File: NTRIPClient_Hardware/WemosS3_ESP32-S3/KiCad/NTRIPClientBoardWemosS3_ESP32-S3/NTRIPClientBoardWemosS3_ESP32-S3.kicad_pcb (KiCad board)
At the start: 2 copper layers, 68.9 x 133 mm, 2 parts, among them U1 Wemos_S3_ESP32-S3

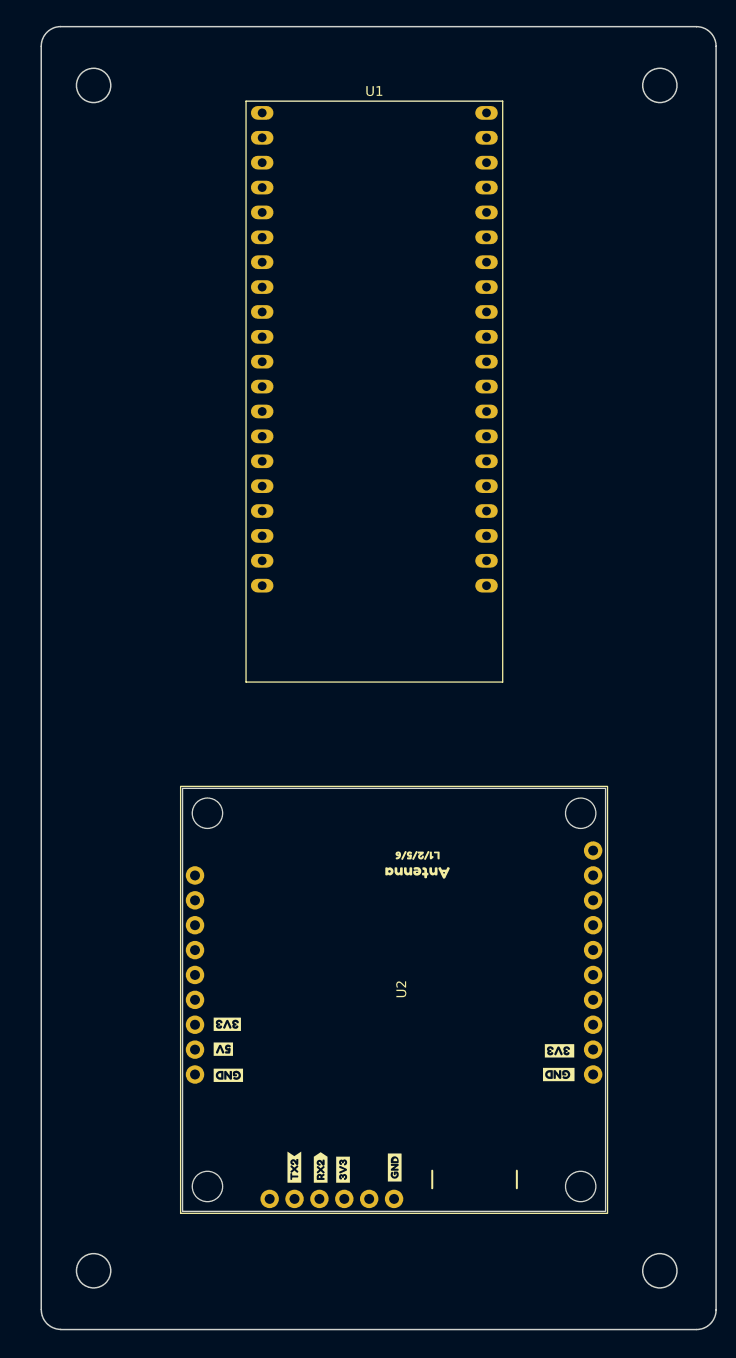
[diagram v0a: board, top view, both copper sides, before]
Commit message: Updated PCB for LOLIN S3 WEMOS board to version 1.0
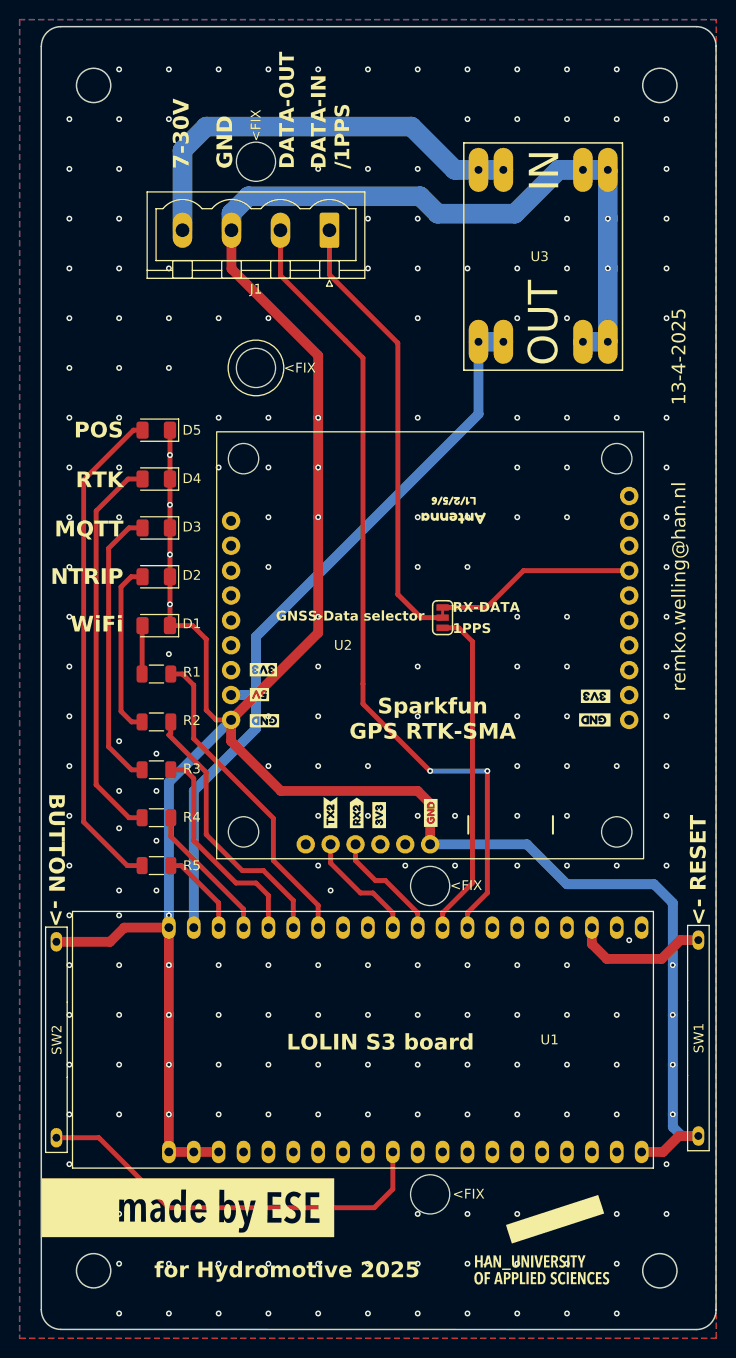
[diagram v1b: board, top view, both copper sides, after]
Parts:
- added D1: GREEN, LED_SMD:LED_1206_3216Metric, F.Cu at (90.2, 97.4)
- added D2: GREEN, LED_SMD:LED_1206_3216Metric, F.Cu at (90.2, 92.4)
- added D3: GREEN, LED_SMD:LED_1206_3216Metric, F.Cu at (90.2, 87.4)
- added D4: YELLOW, LED_SMD:LED_1206_3216Metric, F.Cu at (90.2, 82.5)
- added D5: YELLOW, LED_SMD:LED_1206_3216Metric, F.Cu at (90.2, 77.5)
- added G***: LOGO, my-KiCad-library:HAN_logo_14x19p4, F.Cu at (129.5, 160.0)
- added G***: LOGO, my-KiCad-library:MadeByESE_30x6, F.Cu at (93.3, 156.8)
- added J1: Screw_Terminal_01x04, Connector_Phoenix_MSTB:PhoenixContact_MSTBVA_2,5_4-G_1x04_P5.00mm_Vertical, F.Cu at (107.8, 57.1)
- added JP1: ~, SparkFun-Jumper:Jumper_3_NC-1_Trace, F.Cu at (119.4, 96.6)
- added R1: 1K, Resistor_SMD:R_1206_3216Metric, F.Cu at (90.2, 102.4)
- added R2: 1K, Resistor_SMD:R_1206_3216Metric, F.Cu at (90.2, 107.3)
- added R3: 1K, Resistor_SMD:R_1206_3216Metric, F.Cu at (90.2, 112.1)
- added R4: 1K, Resistor_SMD:R_1206_3216Metric, F.Cu at (90.2, 117.0)
- added R5: 1K, Resistor_SMD:R_1206_3216Metric, F.Cu at (90.2, 121.9)
- added SW1: RESET, my-KiCad-library:SW_SPST_REED_20mm, F.Cu at (145.5, 139.5)
- added SW2: BUTTON, my-KiCad-library:SW_SPST_REED_20mm, F.Cu at (80.0, 139.7)
- added U3: BUCK-30V-5V, my-KiCad-library:BUCK-30V-5V, F.Cu at (129.8, 59.5)
- moved U1 70.6 mm to (115.6, 139.7), turned to 180 degrees
- moved U2 36.4 mm to (119.4, 98.3)
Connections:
- U1 pad 10: unconnected-(U1-17-Pad10) -> /GNSS_RTK_TX
- U1 pad 11: unconnected-(U1-18-Pad11) -> /GNSS_RTK_RX
- U1 pad 14: unconnected-(U1-46-Pad14) -> /LED_WIFI
- U1 pad 15: unconnected-(U1-9-Pad15) -> /LED_NTRIP
- U1 pad 16: unconnected-(U1-10-Pad16) -> /LED_MQTT
- U1 pad 17: unconnected-(U1-11-Pad17) -> /NTRIP_PACKET_LED
- U1 pad 18: unconnected-(U1-12-Pad18) -> /MQTT_PACKET_LED
- U1 pad 3: unconnected-(U1-RESET-Pad3) -> /RESET
- U1 pad 30: unconnected-(U1-0-Pad30) -> /IO0
- U1 pad 8: unconnected-(U1-15-Pad8) -> /ACQ_TX
- U1 pad 9: unconnected-(U1-16-Pad9) -> /ACQ_RX
- U2 pad 11: unconnected-(U2-TX2-Pad11) -> /GNSS_RTK_RX
- U2 pad 12: unconnected-(U2-RX2-Pad12) -> /GNSS_RTK_TX
- U2 pad 22: unconnected-(U2-1PPS-Pad22) -> /1PPS
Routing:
- net /GND: track 0.00 -> 308.1 mm, vias 0 -> 229
- net /ACQ_TX: track 0.00 -> 84.2 mm, vias 0 -> 2
- net /5V: track 0.00 -> 76.9 mm
- net Net-(D5-A): track 0.00 -> 50.8 mm
- net Net-(J1-Pin_1): track 0.00 -> 45.6 mm
- net /7-24V: track 0.00 -> 43.7 mm
- net /IO0: track 0.00 -> 41.9 mm
- net Net-(D4-A): track 0.00 -> 40.1 mm
- net /ACQ_RX: track 0.00 -> 34.1 mm
- net /LED_WIFI: track 0.00 -> 32.8 mm
- net Net-(D3-A): track 0.00 -> 29.0 mm
- net /LED_NTRIP: track 0.00 -> 27.6 mm
- net /LED_MQTT: track 0.00 -> 22.3 mm
- net /1PPS: track 0.00 -> 20.6 mm
- net Net-(D2-A): track 0.00 -> 17.9 mm
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- added copper zone on B.Cu, net /GND
- added copper zone on F.Cu, net /GND
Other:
- outline, holes or cut-outs redrawn
- board text added: "13-4-2025"
- board text added: "1PPS"
- board text added: "7-30V"
- board text added: "<- RESET"
- board text added: "<FIX"
- board text added: "BUTTON ->"
- board text added: "DATA-IN /1PPS"
- board text added: "DATA-OUT"
- board text added: "GND"
- board text added: "GNSS-Data selector"
- board text added: "LOLIN S3 board"
- board text added: "MQTT"
- board text added: "NTRIP"
- board text added: "POS"
- board text added: "RTK"
- board text added: "RX-DATA"
- board text added: "Sparkfun GPS RTK-SMA"
- board text added: "WiFi"
- board text added: "for Hydromotive 2025"
- board text added: "remko.welling@han.nl"
